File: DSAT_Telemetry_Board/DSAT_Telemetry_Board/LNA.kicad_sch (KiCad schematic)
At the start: 1 part

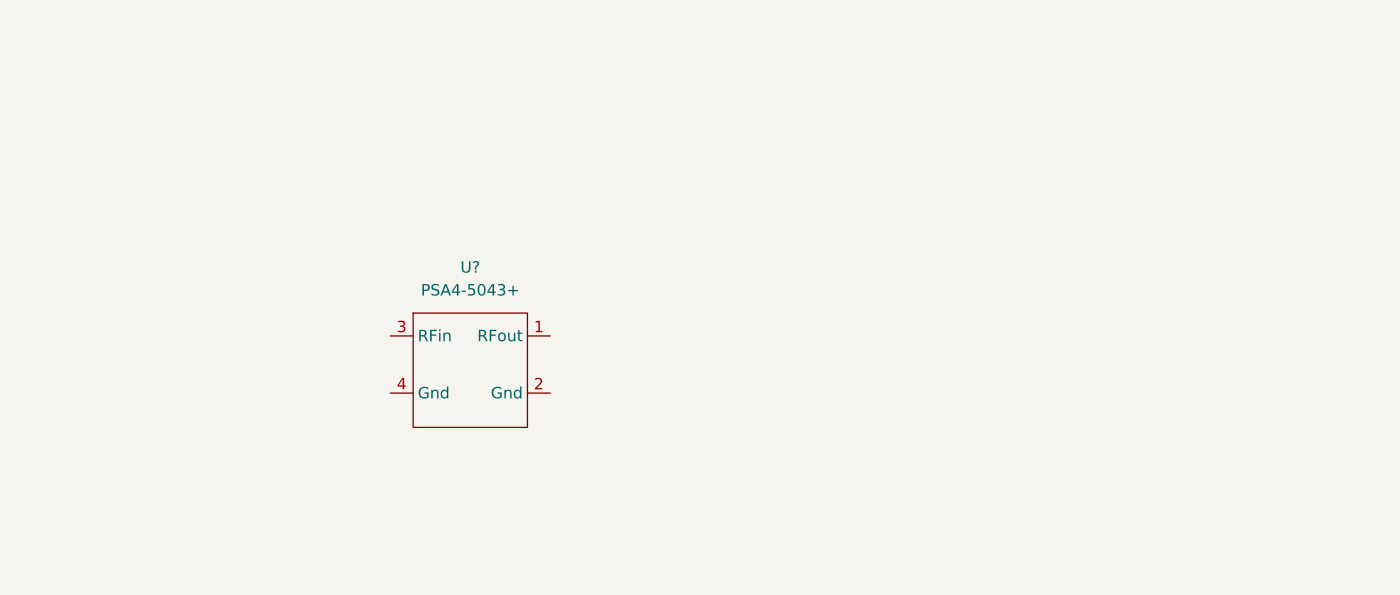
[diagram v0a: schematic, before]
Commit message: Seperate Branch
Updated Pin names, Added LNA, Fixed Pins on USB connection
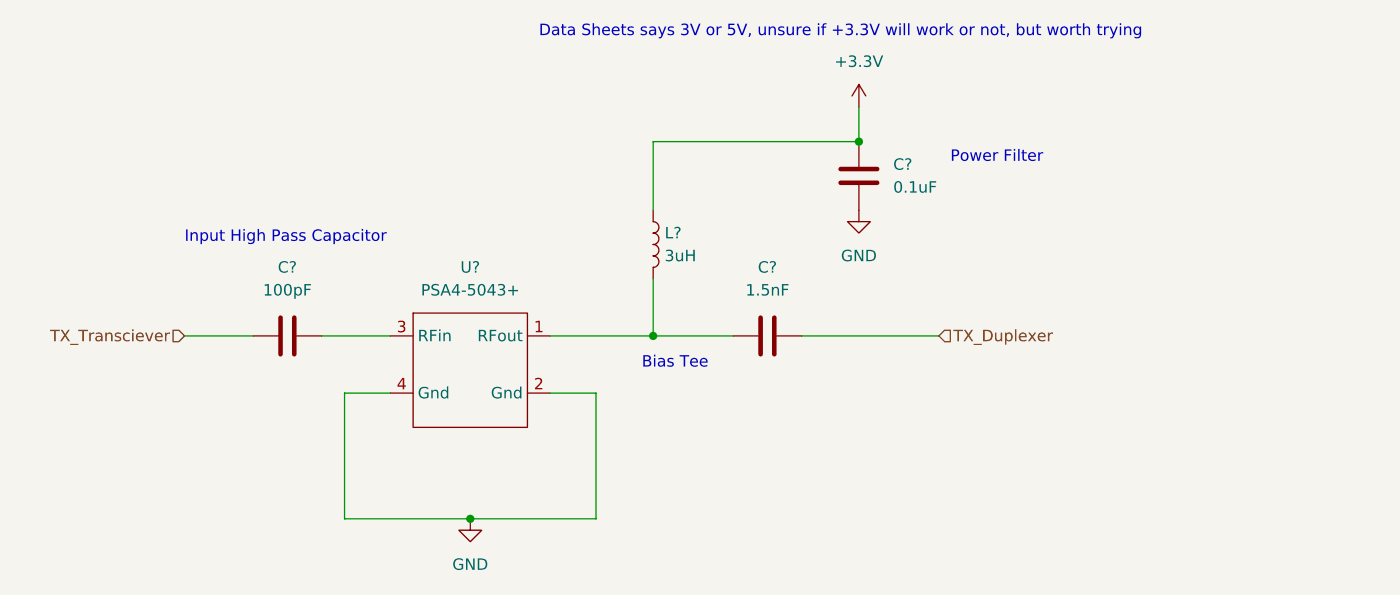
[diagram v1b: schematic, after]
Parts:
- added C?: 0.1uF, symbol Device:C
- added C?: 100pF, symbol Device:C
- added C?: 1.5nF, symbol Device:C
- added L?: 3uH, symbol Device:L
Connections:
- net at U?.1 (RFout): now also C?.1, L?.2
- net GND: now reaches U?.2 (Gnd)
- net GND: now also U?.4 (Gnd), C?.2
- net at U?.3 (RFin): now also C?.2
- new net +3.3V: C?.1, L?.1
- new net TX_Duplexer: C?.2
- new net TX_Transciever: C?.1
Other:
- note added: "Bias Tee"
- note added: "Data Sheets says 3V or 5V, unsure if +3.3V will work or not, but worth trying"
- note added: "Input High Pass Capacitor"
- note added: "Power Filter"
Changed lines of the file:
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@@
 (kicad_sch (version 20211123) (generator eeschema)
   (paper "A4")
+  (junction (at 133.35 111.76) (diameter 0) (color 0 0 0 0)
+  )
+  (junction (at 153.67 91.44) (diameter 0) (color 0 0 0 0)
+  )
+  (junction (at 176.53 69.85) (diameter 0) (color 0 0 0 0)
+  )
+  (wire (pts (xy 116.84 91.44) (xy 124.46 91.44))
+    (stroke (width 0) (type default) (color 0 0 0 0))
+  )
+  (wire (pts (xy 153.67 69.85) (xy 176.53 69.85))
+    (stroke (width 0) (type default) (color 0 0 0 0))
+  )
+  (wire (pts (xy 147.32 97.79) (xy 147.32 111.76))
+    (stroke (width 0) (type default) (color 0 0 0 0))
+  )
+  (wire (pts (xy 170.18 91.44) (xy 185.42 91.44))
+    (stroke (width 0) (type default) (color 0 0 0 0))
+  )
+  (wire (pts (xy 176.53 66.04) (xy 176.53 69.85))
+    (stroke (width 0) (type default) (color 0 0 0 0))
+  )
+  (wire (pts (xy 119.38 111.76) (xy 133.35 111.76))
+    (stroke (width 0) (type default) (color 0 0 0 0))
+  )
+  (wire (pts (xy 153.67 69.85) (xy 153.67 77.47))
+    (stroke (width 0) (type default) (color 0 0 0 0))
+  )
+  (wire (pts (xy 101.6 91.44) (xy 109.22 91.44))
+    (stroke (width 0) (type default) (color 0 0 0 0))
+  )
+  (wire (pts (xy 153.67 91.44) (xy 162.56 91.44))
+    (stroke (width 0) (type default) (color 0 0 0 0))
+  )
+  (wire (pts (xy 147.32 111.76) (xy 133.35 111.76))
+    (stroke (width 0) (type default) (color 0 0 0 0))
+  )
+  (wire (pts (xy 119.38 97.79) (xy 119.38 111.76))
+    (stroke (width 0) (type default) (color 0 0 0 0))
+  )
+  (wire (pts (xy 153.67 85.09) (xy 153.67 91.44))
+    (stroke (width 0) (type default) (color 0 0 0 0))
+  )
+  (wire (pts (xy 124.46 97.79) (xy 119.38 97.79))
+    (stroke (width 0) (type default) (color 0 0 0 0))
+  )
+  (wire (pts (xy 147.32 97.79) (xy 142.24 97.79))
+    (stroke (width 0) (type default) (color 0 0 0 0))
+  )
+  (wire (pts (xy 142.24 91.44) (xy 153.67 91.44))
+    (stroke (width 0) (type default) (color 0 0 0 0))
+  )
+  (text "Input High Pass Capacitor\n" (at 101.6 81.28 0)
+    (effects (font (size 1.27 1.27)) (justify left bottom))
+  )
+  (text "Bias Tee\n" (at 152.4 95.25 0)
+    (effects (font (size 1.27 1.27)) (justify left bottom))
+  )
+  (text "Data Sheets says 3V or 5V, unsure if +3.3V will work or not, but worth trying\n"
+    (at 140.97 58.42 0)
+    (effects (font (size 1.27 1.27)) (justify left bottom))
+  )
+  (text "Power Filter\n" (at 186.69 72.39 0)
+    (effects (font (size 1.27 1.27)) (justify left bottom))
+  )
+  (hierarchical_label "TX_Transciever" (shape input) (at 101.6 91.44 180)
+    (effects (font (size 1.27 1.27)) (justify right))
+  )
+  (hierarchical_label "TX_Duplexer" (shape input) (at 185.42 91.44 0)
+    (effects (font (size 1.27 1.27)) (justify left))
+  )
+  (symbol (lib_id "Device:C") (at 176.53 73.66 0) (unit 1)
+    (in_bom yes) (on_board yes) (fields_autoplaced)
+    (property "Reference" "C?" (id 0) (at 180.34 72.3899 0)
+      (effects (font (size 1.27 1.27)) (justify left))
+    )
+    (property "Value" "0.1uF" (id 1) (at 180.34 74.9299 0)
+      (effects (font (size 1.27 1.27)) (justify left))
+    )
+    (property "Footprint" "" (id 2) (at 177.4952 77.47 0)
+      (effects (font (size 1.27 1.27)) hide)
+    )
+    (property "Datasheet" "~" (id 3) (at 176.53 73.66 0)
+      (effects (font (size 1.27 1.27)) hide)
+    )
+    (pin "1")
+    (pin "2")
+  )
+  (symbol (lib_id "power:+3.3V") (at 176.53 66.04 0) (unit 1)
+    (in_bom yes) (on_board yes) (fields_autoplaced)
+    (property "Reference" "#PWR?" (id 0) (at 176.53 69.85 0)
+      (effects (font (size 1.27 1.27)) hide)
+    )
+    (property "Value" "+3.3V" (id 1) (at 176.53 60.96 0))
+    (property "Footprint" "" (id 2) (at 176.53 66.04 0)
+      (effects (font (size 1.27 1.27)) hide)
+    )
+    (property "Datasheet" "" (id 3) (at 176.53 66.04 0)
+      (effects (font (size 1.27 1.27)) hide)
+    )
+    (pin "1")
+  )
+  (symbol (lib_id "Device:C") (at 113.03 91.44 90) (mirror x) (unit 1)
+    (in_bom yes) (on_board yes) (fields_autoplaced)
+    (property "Reference" "C?" (id 0) (at 113.03 83.82 90))
+    (property "Value" "100pF" (id 1) (at 113.03 86.36 90))
+    (property "Footprint" "" (id 2) (at 116.84 92.4052 0)
+      (effects (font (size 1.27 1.27)) hide)
+    )
+    (property "Datasheet" "~" (id 3) (at 113.03 91.44 0)
+      (effects (font (size 1.27 1.27)) hide)
+    )
+    (pin "1")
+    (pin "2")
+  )
+  (symbol (lib_id "power:GND") (at 176.53 77.47 0) (unit 1)
+    (in_bom yes) (on_board yes) (fields_autoplaced)
+    (property "Reference" "#PWR?" (id 0) (at 176.53 83.82 0)
+      (effects (font (size 1.27 1.27)) hide)
+    )
+    (property "Value" "GND" (id 1) (at 176.53 82.55 0))
+    (property "Footprint" "" (id 2) (at 176.53 77.47 0)
+      (effects (font (size 1.27 1.27)) hide)
+    )
+    (property "Datasheet" "" (id 3) (at 176.53 77.47 0)
+      (effects (font (size 1.27 1.27)) hide)
+    )
+    (pin "1")
+  )
+  (symbol (lib_id "Device:L") (at 153.67 81.28 0) (unit 1)
+    (in_bom yes) (on_board yes) (fields_autoplaced)
+    (property "Reference" "L?" (id 0) (at 154.94 80.0099 0)
+      (effects (font (size 1.27 1.27)) (justify left))
+    )
+    (property "Value" "3uH" (id 1) (at 154.94 82.5499 0)
+      (effects (font (size 1.27 1.27)) (justify left))
+    )
+    (property "Footprint" "" (id 2) (at 153.67 81.28 0)
+      (effects (font (size 1.27 1.27)) hide)
+    )
+    (property "Datasheet" "~" (id 3) (at 153.67 81.28 0)
+      (effects (font (size 1.27 1.27)) hide)
+    )
+    (pin "1")
+    (pin "2")
+  )
+  (symbol (lib_id "Device:C") (at 166.37 91.44 90) (mirror x) (unit 1)
+    (in_bom yes) (on_board yes) (fields_autoplaced)
+    (property "Reference" "C?" (id 0) (at 166.37 83.82 90))
+    (property "Value" "1.5nF" (id 1) (at 166.37 86.36 90))
+    (property "Footprint" "" (id 2) (at 170.18 92.4052 0)
+      (effects (font (size 1.27 1.27)) hide)
+    )
+    (property "Datasheet" "~" (id 3) (at 166.37 91.44 0)
+      (effects (font (size 1.27 1.27)) hide)
+    )
+    (pin "1")
+    (pin "2")
+  )
   (symbol (lib_id "DSAT_Telemetry_Libraries:PSA4-5043+") (at 133.35 83.82 0) (unit 1)
     (in_bom yes) (on_board yes) (fields_autoplaced)
@@
     (pin "4")
   )
+  (symbol (lib_id "power:GND") (at 133.35 111.76 0) (unit 1)
+    (in_bom yes) (on_board yes) (fields_autoplaced)
+    (property "Reference" "#PWR?" (id 0) (at 133.35 118.11 0)
+      (effects (font (size 1.27 1.27)) hide)
+    )
+    (property "Value" "GND" (id 1) (at 133.35 116.84 0))
+    (property "Footprint" "" (id 2) (at 133.35 111.76 0)
+      (effects (font (size 1.27 1.27)) hide)
+    )
+    (property "Datasheet" "" (id 3) (at 133.35 111.76 0)
+      (effects (font (size 1.27 1.27)) hide)
+    )
+    (pin "1")
+  )
 )
